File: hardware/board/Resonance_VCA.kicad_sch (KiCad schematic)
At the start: 31 parts

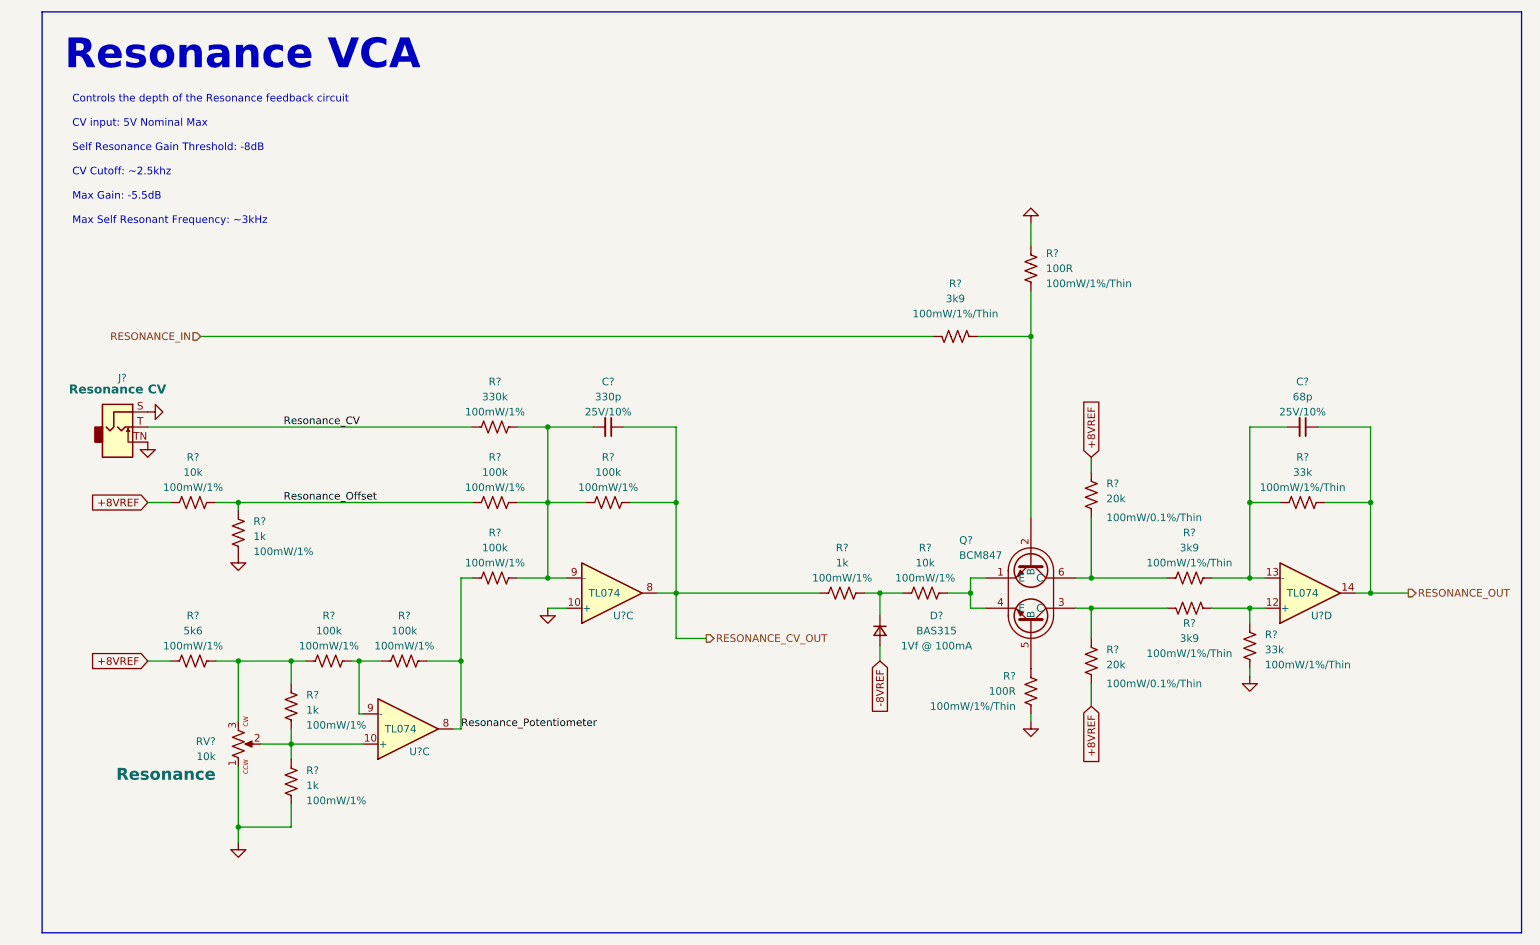
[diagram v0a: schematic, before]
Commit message: Updated Schematic
-Added R935, R936, and Q901 to make resonance self oscillation LED turn on sharply

-Moved D929, D930, and added R933, R934 to make FM1 LED more sensitive

-Changed FM1 Attenuverter and added R410 and R411 to make FM1 Knob have some curve/deadzone

-Changed Resonance VCA output and added R623 and R624 to make resonance VCA output higher voltage to avoid opamp offset being significant .

-Added testing documents
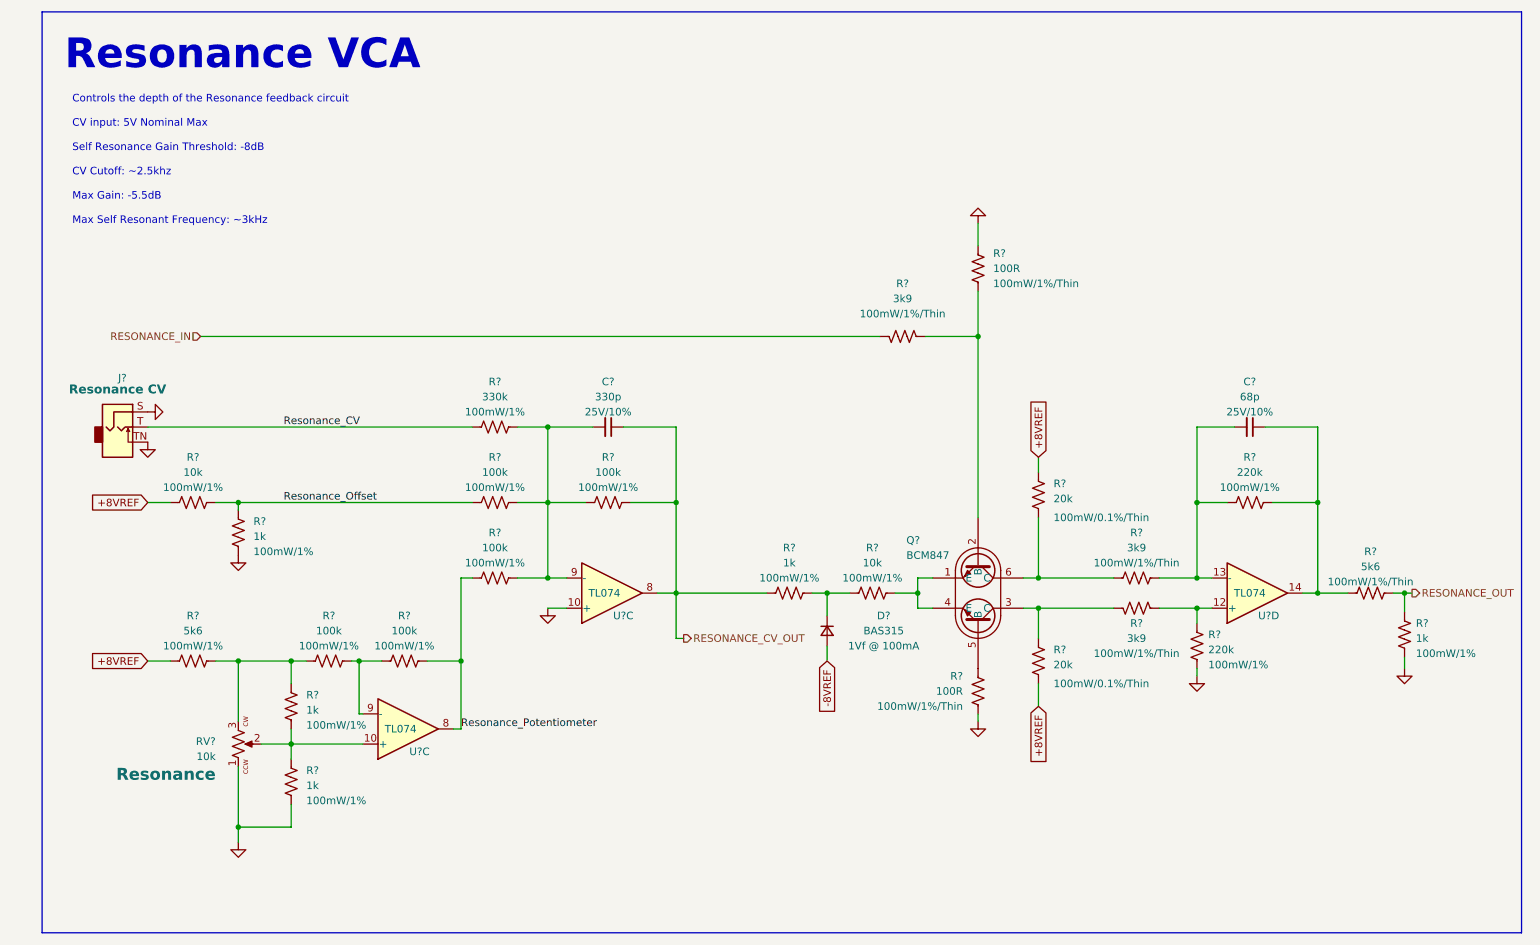
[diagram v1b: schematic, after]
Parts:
- removed R? (x2): 33k, winterbloom:R_0603_HandSolder, symbol Device:R_US
- added R? (x2): 220k, winterbloom:R_0603_HandSolder, symbol Device:R_US
- added R?: 1k, winterbloom:R_0603_HandSolder, symbol Device:R_US
- added R?: 5k6, winterbloom:R_0603_HandSolder, symbol Device:R_US
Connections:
- net GND: now also R?.2, R?.2
- net RESONANCE_OUT: now also R?.1, R?.2; no longer C?.1, U?.14
- net at R?.1, U?.12 (+): now also R?.1
- net at C?.2, R?.1, U?.13 (-): now also R?.2
- new net: C?.1, R?.1, R?.1, U?.14
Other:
- moved on the sheet: C?, D?, Q?, R?, U?D

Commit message: Slight tweaks
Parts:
- removed C?: 68p, winterbloom:C_0603_HandSolder, symbol Device:C_Small
- added C?: 10p, winterbloom:C_0603_HandSolder, symbol Device:C_Small
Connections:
- net at R?.1, R?.1, U?.14: now also C?.2
- net at R?.1, R?.2, U?.13 (-): now also C?.1
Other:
- note added: "Controls the depth of the Resonance feedback circuit CV input: 5V Nominal Max Self Resonance Gain Threshold: -8dB CV Cutoff: ~2.5khz Max Gain: -5.5dB Max Self Resonant Frequency: ~16kHz"
- note removed: "Controls the depth of the Resonance feedback circuit CV input: 5V Nominal Max Self Resonance Gain Threshold: -8dB CV Cutoff: ~2.5khz Max Gain: -5.5dB Max Self Resonant Frequency: ~3kHz"
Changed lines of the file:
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@@
     (effects (font (size 5 5) (thickness 0.508) bold) (justify left bottom))
   )
-  (text "Controls the depth of the Resonance feedback circuit \n\nCV input: 5V Nominal Max\n\nSelf Resonance Gain Threshold: -8dB\n\nCV Cutoff: ~2.5khz\n\nMax Gain: -5.5dB\n\nMax Self Resonant Frequency: ~3kHz\n\n\n"
+  (text "Controls the depth of the Resonance feedback circuit \n\nCV input: 5V Nominal Max\n\nSelf Resonance Gain Threshold: -8dB\n\nCV Cutoff: ~2.5khz\n\nMax Gain: -5.5dB\n\nMax Self Resonant Frequency: ~16kHz\n\n\n"
     (at 20.32 55.245 0)
     (effects (font (size 1.27 1.27)) (justify left bottom))
@@
     )
   )
+  (symbol (lib_id "Device:C_Small") (at 218.44 85.09 90) (unit 1)
+    (in_bom yes) (on_board yes) (dnp no) (fields_autoplaced)
+    (property "Reference" "C?" (at 218.4463 77.47 90)
+      (effects (font (size 1.27 1.27)))
+    )
+    (property "Value" "10p" (at 218.4463 80.01 90)
+      (effects (font (size 1.27 1.27)))
+    )
+    (property "Footprint" "winterbloom:C_0603_HandSolder" (at 218.44 85.09 0)
+      (effects (font (size 1.27 1.27)) hide)
+    )
+    (property "Datasheet" "~" (at 218.44 85.09 0)
+      (effects (font (size 1.27 1.27)) hide)
+    )
+    (property "Notes" "" (at 218.44 85.09 0)
+      (effects (font (size 1.27 1.27)) hide)
+    )
+    (property "Rating" "25V/10%" (at 218.4463 82.55 90)
+      (effects (font (size 1.27 1.27)))
+    )
+    (pin "1")
+    (pin "2")
+    (instances
+      (project "board"
+        (path "/55082cc1-c956-45a6-b2b5-3db02a6da9d0"
+          (reference "C?") (unit 1)
+        )
+      )
+      (project "mainboard"
+        (path "/960bd036-bf0c-45ea-9f41-1321756e0e5a/2f882567-d4bc-4d02-ab1f-fc30e1722a04"
+          (reference "C802") (unit 1)
+        )
+        (path "/960bd036-bf0c-45ea-9f41-1321756e0e5a/48d891c0-35ba-4c8e-a930-c990a10298eb"
+          (reference "C602") (unit 1)
+        )
+      )
+      (project "VCA"
+        (path "/de69ad6f-07bb-4f9c-962b-520f6532317d"
+          (reference "C?") (unit 1)
+        )
+        (path "/de69ad6f-07bb-4f9c-962b-520f6532317d/5e672b4f-6fd9-484e-977a-c1eaf1352b32"
+          (reference "C?") (unit 1)
+        )
+      )
+    )
+  )
   (symbol (lib_id "power:GND") (at 209.55 127 0) (unit 1)
     (in_bom yes) (on_board yes) (dnp no) (fields_autoplaced)
@@
         )
       )
-    )
-  )
-  (symbol (lib_id "Device:C_Small") (at 218.44 85.09 270) (unit 1)
-    (in_bom yes) (on_board yes) (dnp no) (fields_autoplaced)
-    (property "Reference" "C?" (at 218.4336 77.47 90)
-      (effects (font (size 1.27 1.27)))
-    )
-    (property "Value" "68p" (at 218.4336 80.01 90)
-      (effects (font (size 1.27 1.27)))
-    )
-    (property "Footprint" "winterbloom:C_0603_HandSolder" (at 218.44 85.09 0)
-      (effects (font (size 1.27 1.27)) hide)
-    )
-    (property "Datasheet" "~" (at 218.44 85.09 0)
-      (effects (font (size 1.27 1.27)) hide)
-    )
-    (property "Notes" "" (at 218.44 85.09 0)
-      (effects (font (size 1.27 1.27)) hide)
-    )
-    (property "Rating" "25V/10%" (at 218.4336 82.55 90)
-      (effects (font (size 1.27 1.27)))
-    )
-    (pin "1")
-    (pin "2")
-    (instances
-      (project "board"
-        (path "/55082cc1-c956-45a6-b2b5-3db02a6da9d0"
-          (reference "C?") (unit 1)
-        )
-      )
-      (project "mainboard"
-        (path "/960bd036-bf0c-45ea-9f41-1321756e0e5a"
-          (reference "C?") (unit 1)
-        )
-        (path "/960bd036-bf0c-45ea-9f41-1321756e0e5a/3b1fa3f2-493c-449c-a2d6-10ea677680a0"
-          (reference "C?") (unit 1)
-        )
-        (path "/960bd036-bf0c-45ea-9f41-1321756e0e5a/48d891c0-35ba-4c8e-a930-c990a10298eb"
-          (reference "C602") (unit 1)
-        )
-      )

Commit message: hardware: clear ERC issues, move BCM847 to the Winterbloom symbol library
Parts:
- Q?: symbol Carson's Schematic Symbols:BCM847 -> winterbloom:BCM847
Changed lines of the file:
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@@
     )
   )
-  (symbol (lib_id "Carson's Schematic Symbols:BCM847") (at 172.72 113.03 270) (unit 1)
+  (symbol (lib_id "winterbloom:BCM847") (at 172.72 113.03 270) (unit 1)
     (in_bom yes) (on_board yes) (dnp no)
     (property "Reference" "Q?" (at 160.655 104.14 90)
@@
       (effects (font (size 1.27 1.27)) (justify left))
     )
-    (property "Footprint" "Package_TO_SOT_SMD:SOT-363_SC-70-6" (at 184.785 113.03 0)
+    (property "Footprint" "Package_TO_SOT_SMD:SOT-363_SC-70-6" (at 172.72 113.03 0)
       (effects (font (size 1.27 1.27)) hide)
     )
-    (property "Datasheet" "" (at 184.785 113.03 0)
+    (property "Datasheet" "https://assets.nexperia.com/documents/data-sheet/BCM847BS.pdf" (at 172.72 113.03 0)
       (effects (font (size 1.27 1.27)) hide)
     )

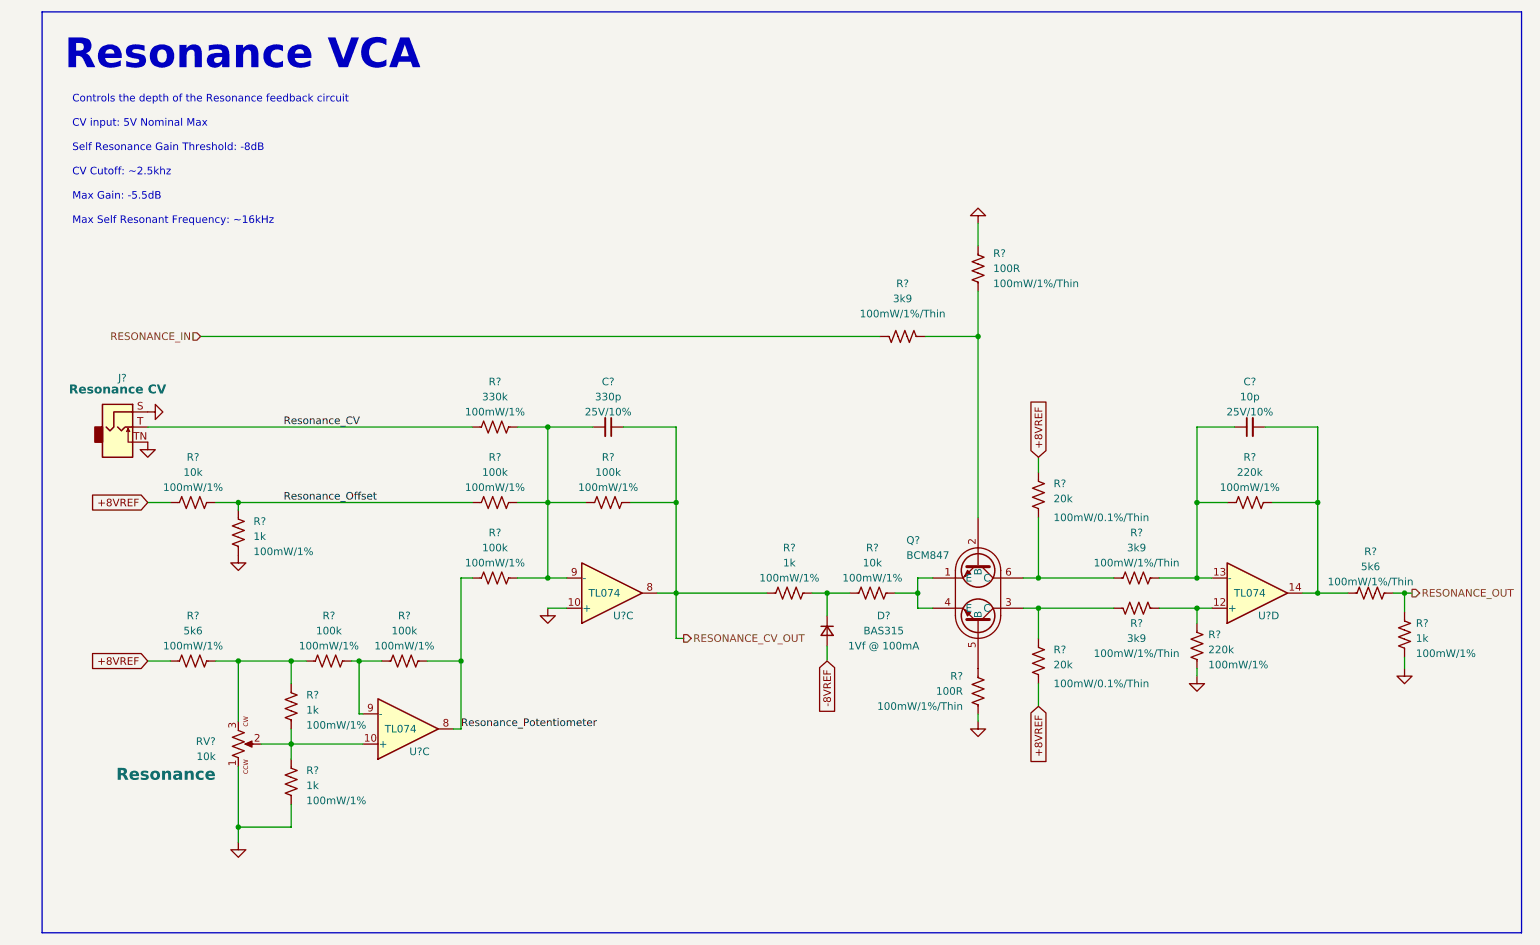
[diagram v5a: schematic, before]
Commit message: hardware: add MPNs, DigiKey part numbers, and LCSC part numbers for all BOM items
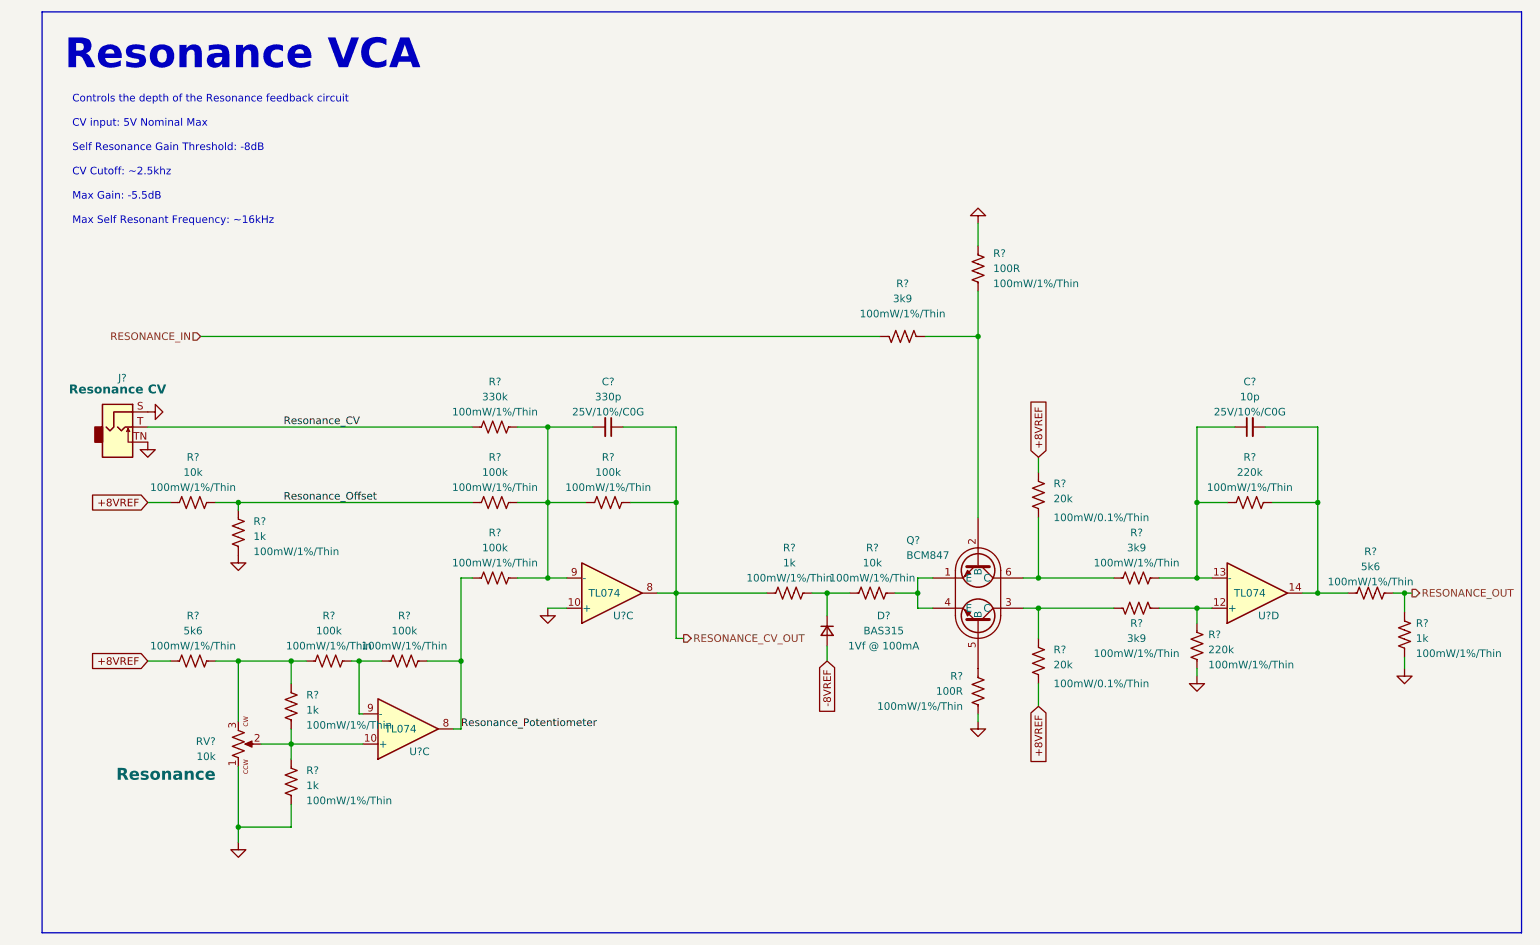
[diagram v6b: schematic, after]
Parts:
- C?: DigiKey (none) -> 1276-1027-1-ND; LCSC (none) -> C1634; MPN (none) -> CL10C100JB8NNNC; Rating 25V/10% -> 25V/10%/C0G; Substitutes Allowed (none) -> Yes
- C?: DigiKey (none) -> 1276-1073-1-ND; LCSC (none) -> C1664; MPN (none) -> CL10C331JB8NNNC; Rating 25V/10% -> 25V/10%/C0G; Substitutes Allowed (none) -> Yes
- D?: DigiKey (none) -> 1727-4309-2-ND; LCSC (none) -> C109218; Substitutes Allowed (none) -> No
- Q?: Attention ! -> (none); DigiKey (none) -> 1727-5456-1-ND; LCSC (none) -> C396099; Substitutes Allowed (none) -> No
- R? (x2): DigiKey (none) -> YAG2321CT-ND; LCSC (none) -> C469659; MPN (none) -> RT0603FRE0710KL; Rating 100mW/1% -> 100mW/1%/Thin; Substitutes Allowed (none) -> Yes
- R? (x2): DigiKey (none) -> YAG5946CT-ND; LCSC (none) -> C706140; MPN (none) -> RT0603FRE07220KL; Rating 100mW/1% -> 100mW/1%/Thin; Substitutes Allowed (none) -> Yes
- R? (x5): DigiKey (none) -> 13-RT0603FRE13100KLTR-ND; LCSC (none) -> C4107493; MPN (none) -> RT0603FRE13100KL; Rating 100mW/1% -> 100mW/1%/Thin; Substitutes Allowed (none) -> Yes
- R? (x5): DigiKey (none) -> YAG2323TR-ND; LCSC (none) -> C375503; MPN (none) -> RT0603FRE071KL; Rating 100mW/1% -> 100mW/1%/Thin; Substitutes Allowed (none) -> Yes
- R? (x2): DigiKey (none) -> YAG1582CT-ND; LCSC (none) -> C723637; MPN (none) -> RT0603BRD0720KL; Substitutes Allowed (none) -> Ask
- R? (x2): DigiKey (none) -> YAG1497CT-ND; LCSC (none) -> C122970; MPN (none) -> RT0603BRD07100RL; Substitutes Allowed (none) -> Ask
- R? (x3): DigiKey (none) -> YAG5961CT-ND; LCSC (none) -> C863790; MPN (none) -> RT0603FRE073K9L; Substitutes Allowed (none) -> Yes
- R?: DigiKey (none) -> 13-RT0603FRE075K6LCT-ND; LCSC (none) -> C706186; MPN (none) -> RT0603FRE075K6L; Substitutes Allowed (none) -> Yes
- R?: DigiKey (none) -> 13-RT0603FRE07330KLCT-ND; LCSC (none) -> C863745; MPN (none) -> RT0603FRE07330KL; Rating 100mW/1% -> 100mW/1%/Thin; Substitutes Allowed (none) -> Yes
- R?: DigiKey (none) -> 13-RT0603FRE075K6LCT-ND; LCSC (none) -> C706186; MPN (none) -> RT0603FRE075K6L; Rating 100mW/1% -> 100mW/1%/Thin; Substitutes Allowed (none) -> Yes
- U? (x3): DigiKey (none) -> 296-7198-1-ND; LCSC (none) -> C96507; MPN TL074CPW -> TL074CPWR; Substitutes Allowed (none) -> No
